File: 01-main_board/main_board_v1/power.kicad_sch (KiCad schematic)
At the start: 20 parts, among them IC1 MAX6105EUR+T, IC2 LP5907MFX-2.5_NOPB, IC3 L78M05ABDT-TR, IC4 SPX3819S-L_TR, U4 TPS2115APWR

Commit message: finished analog input traces
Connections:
- net GNDA is gone; now on net PGND: C38.2, C39.1, C41.1, C7.1, R45.2
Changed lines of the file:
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@@
 			)
 		)
-		(property "Value" "GNDA"
+		(property "Value" "PGND"
 			(at 127 121.92 0)
 			(effects
@@
 			)
 		)
-		(property "Value" "GNDA"
+		(property "Value" "PGND"
 			(at 78.74 63.5 0)
 			(effects
@@
 			)
 		)
-		(property "Value" "GNDA"
+		(property "Value" "PGND"
 			(at 124.46 93.98 0)
 			(effects
@@
 			)
 		)
-		(property "Value" "GNDA"
+		(property "Value" "PGND"
 			(at 76.2 95.25 0)
 			(effects
@@
 			)
 		)
-		(property "Value" "GNDA"
+		(property "Value" "PGND"
 			(at 76.2 118.11 0)
 			(effects

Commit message: resolved all non-GND related DRC issues in layout
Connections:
- net 3V3: no longer C1.1, IC2.1 (IN), IC2.3 (EN)
- new net 3V3_teensy: C1.1, IC2.1 (IN), IC2.3 (EN)
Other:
- moved on the sheet: D1
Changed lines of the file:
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@@
 	(text "ESP32 recommends 3.3V power supply with >= 500 mA supply current, \n\nESP32C6 or ESP32S3 specifically, dobule check datasheets\n"
 		(exclude_from_sim no)
-		(at 235.712 143.256 0)
+		(at 255.27 141.732 0)
 		(effects
 			(font
@@
 	(text "Vout = 1.235(1 + R1/R2), 22k < r2 < 47k, lower r1 to round\noutput capacitor is 2.2uF if alunimum and 1 uF if tantalum"
 		(exclude_from_sim no)
-		(at 237.49 107.95 0)
+		(at 251.46 133.096 0)
 		(effects
 			(font
@@
 	(text "Note: 2.5V Reference supplied by DAC"
 		(exclude_from_sim no)
-		(at 189.23 76.962 0)
+		(at 182.372 79.756 0)
 		(effects
 			(font
@@
 		)
 	)
-	(global_label "3V3"
+	(global_label "3V3_teensy"
 		(shape input)
 		(at 115.57 71.12 180)
@@
 		)
 		(property "Intersheetrefs" "${INTERSHEET_REFS}"
-			(at 109.0772 71.12 0)
-			(effects
-				(font
-					(size 1.27 1.27)
-				)
-				(justify right)
-				(hide yes)
-			)
-		)
-	)
-	(global_label "3V3"
+			(at 102.062 71.12 0)
+			(effects
+				(font
+					(size 1.27 1.27)
+				)
+				(justify right)
+				(hide yes)
+			)
+		)
+	)
+	(global_label "3V3_teensy"
 		(shape input)
-		(at 127 76.2 180)
-		(fields_autoplaced yes)
-		(effects
-			(font
-				(size 1.27 1.27)
-			)
-			(justify right)
-		)
-		(property "Intersheetrefs" "${INTERSHEET_REFS}"
-			(at 120.5072 76.2 0)
+		(at 127 76.2 270)
+		(fields_autoplaced yes)
+		(effects
+			(font
+				(size 1.27 1.27)
+			)
+			(justify right)
+		)
+		(property "Intersheetrefs" "${INTERSHEET_REFS}"
+			(at 127 89.708 90)
 			(effects
 				(font
@@
 	(global_label "11.1V"
 		(shape output)
-		(at 55.88 40.64 0)
+		(at 93.98 52.07 0)
 		(fields_autoplaced yes)
 		(effects
@@
 		)
 		(property "Intersheetrefs" "${INTERSHEET_REFS}"
-			(at 64.1871 40.64 0)
+			(at 102.2871 52.07 0)
 			(effects
 				(font
@@
 	(global_label "11.1V_battery"
 		(shape input)
-		(at 48.26 40.64 180)
-		(fields_autoplaced yes)
-		(effects
-			(font
-				(size 1.27 1.27)
-			)
-			(justify right)
-		)
-		(property "Intersheetrefs" "${INTERSHEET_REFS}"
-			(at 32.3935 40.64 0)
+		(at 86.36 52.07 180)
+		(fields_autoplaced yes)
+		(effects
+			(font
+				(size 1.27 1.27)
+			)
+			(justify right)
+		)
+		(property "Intersheetrefs" "${INTERSHEET_REFS}"
+			(at 70.4935 52.07 0)
 			(effects
 				(font
@@
 	(symbol
 		(lib_id "Device:D_Schottky")
-		(at 52.07 40.64 180)
+		(at 90.17 52.07 180)
 		(unit 1)
 		(exclude_from_sim no)
@@
 		(fields_autoplaced yes)
 		(property "Reference" "D1"
-			(at 52.3875 34.29 0)
+			(at 90.4875 45.72 0)
 			(effects
 				(font
@@
 		)
 		(property "Value" "D_Schottky"
-			(at 52.3875 36.83 0)
+			(at 90.4875 48.26 0)
 			(effects
 				(font
@@
 		)
 		(property "Footprint" "Diode_SMD:D_2114_3652Metric"
-			(at 52.07 40.64 0)
+			(at 90.17 52.07 0)
 			(effects
 				(font
@@
 		)
 		(property "Datasheet" "~"
-			(at 52.07 40.64 0)
+			(at 90.17 52.07 0)
 			(effects
 				(font
@@
 		)
 		(property "Description" "Schottky diode"
-			(at 52.07 40.64 0)
-			(effects
-				(font
+			(at 90.17 52.07 0)
+			(effects
+				(font

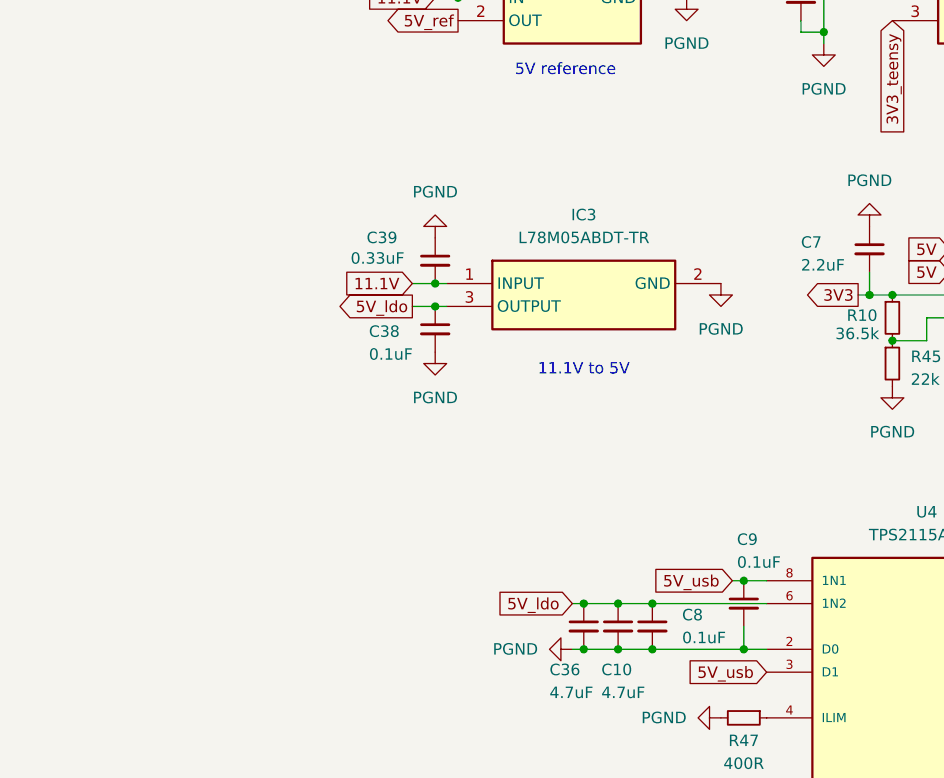
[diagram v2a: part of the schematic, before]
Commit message: changed 5V ldo to 5V buck
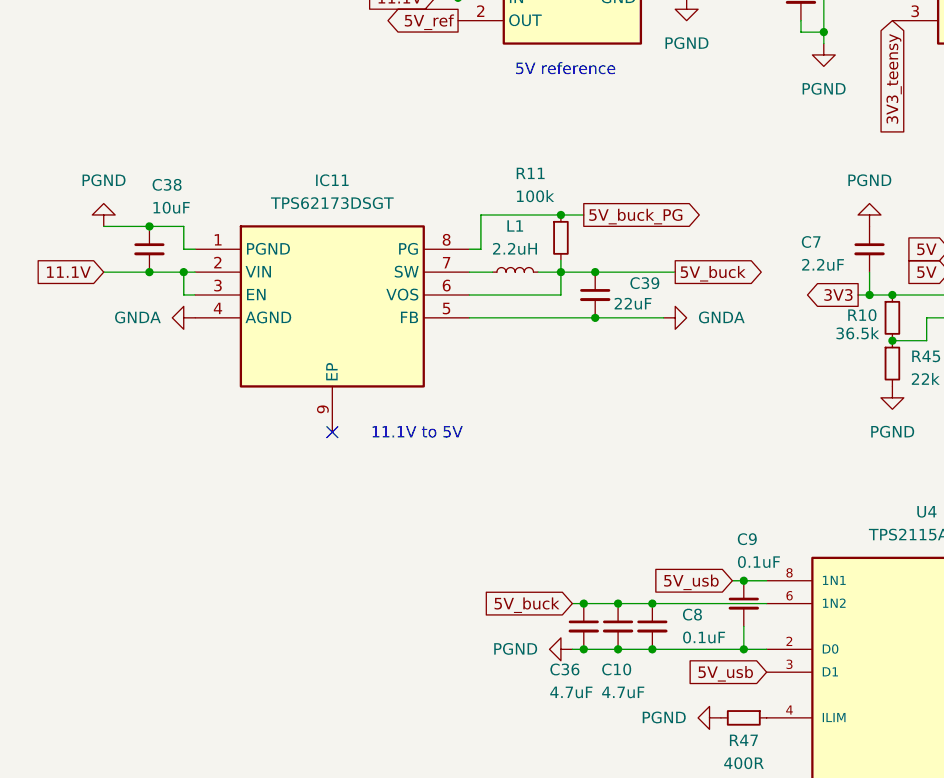
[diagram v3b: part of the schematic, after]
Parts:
- removed IC3: L78M05ABDT-TR, L78M05ABDTTR, symbol 22XT_Main:L78M05ABDT-TR
- added IC11: TPS62173DSGT, 22XT_Main:SON50P200X200X80-9N, symbol 22XT_Main:TPS62173DSGT
- added L1: 2.2uH, Inductor_SMD:L_0402_1005Metric, symbol Device:L_Small
- added R11: 100k, Resistor_SMD:R_0402_1005Metric, symbol Device:R_Small
- C38: value 0.1uF -> 10uF
- C39: value 0.33uF -> 22uF
- D1: footprint Diode_SMD:D_2114_3652Metric -> Diode_SMD:D_0402_1005Metric
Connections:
- net 11.1V: now also C38.2, IC11.2 (VIN), IC11.3 (EN); no longer C39.2
- net PGND: now also C38.1, IC11.1 (PGND); no longer C38.2, C39.1
- net 5V_ldo renamed 5V_buck
- net 5V_buck: now also C39.1, IC11.6 (VOS), L1.2, R11.2; no longer C38.1
- new net: IC11.7 (SW), L1.1
- new net 5V_buck_PG: IC11.8 (PG), R11.1
- new net GNDA: C39.2, IC11.4 (AGND), IC11.5 (FB)
- no-connect marks 0 -> 1
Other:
- moved on the sheet: C38, C39

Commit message: Emma revision
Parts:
- added NT1: NetTie_2, symbol Device:NetTie_2
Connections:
- net GNDA: now also NT1.1
- net PGND renamed B-
- net B-: now also NT1.2
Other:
- note added: "11.1V to 5V buck converter"
- note added: "3.3V to 2.5V LDO"
- note added: "5V to 3.3V LDO"
- note removed: "11.1V to 5V"
- note removed: "3.3V to 2.5V"
- note removed: "5V to 3.3V"

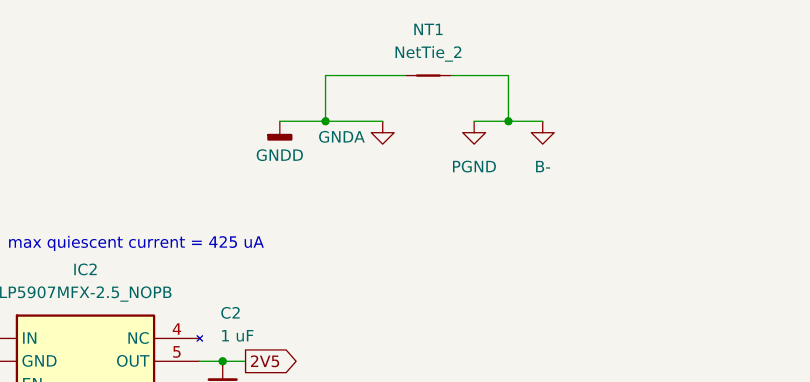
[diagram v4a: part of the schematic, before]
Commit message: Added main board footprint library
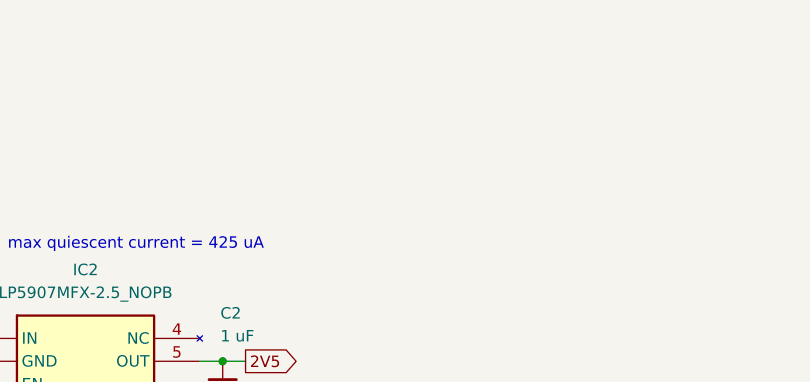
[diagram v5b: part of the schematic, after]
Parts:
- removed NT1: NetTie_2, symbol Device:NetTie_2
- IC1: footprint SOT95P229X119-3N -> (none)
- IC2: footprint SOT95P280X145-5N -> (none)
- IC4: footprint SOIC127P600X175-8N -> (none)
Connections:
- net B- renamed PGND

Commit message: Added new commit
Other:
- note added: "LSM115JE3/TR13:"
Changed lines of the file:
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@@
 	(generator_version "9.0")
 	(paper "A4")
+	(text "LSM115JE3/TR13:"
+		(exclude_from_sim no)
+		(at 91.186 42.926 0)
+		(effects
+			(font
+				(size 1.27 1.27)
+			)
+		)
+	)
 	(text "5V to 3.3V\nLDO"
 		(exclude_from_sim no)

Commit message: Re-assigned all footprints
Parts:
- D1: footprint Diode_SMD:D_0402_1005Metric -> 22XT_Main:DO-214BA_MCH
- IC1: footprint (none) -> Package_TO_SOT_SMD:SOT-23-3
- IC2: footprint (none) -> Package_TO_SOT_SMD:SOT-23-5
- IC4: footprint (none) -> 22XT_Main:SOIC127P600X175-8N
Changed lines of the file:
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@@
 			)
 		)
-		(property "Footprint" "Diode_SMD:D_0402_1005Metric"
+		(property "Footprint" "22XT_Main:DO-214BA_MCH"
 			(at 90.17 52.07 0)
 			(effects
@@
 			)
 		)
-		(property "Footprint" ""
+		(property "Footprint" "Package_TO_SOT_SMD:SOT-23-3"
 			(at 100.33 168.58 0)
 			(effects
@@
 			)
 		)
-		(property "Footprint" ""
+		(property "Footprint" "Package_TO_SOT_SMD:SOT-23-5"
 			(at 148.59 166.04 0)
 			(effects
@@
 			)
 		)
-		(property "Footprint" ""
+		(property "Footprint" "22XT_Main:SOIC127P600X175-8N"
 			(at 160.02 196.52 0)
 			(effects

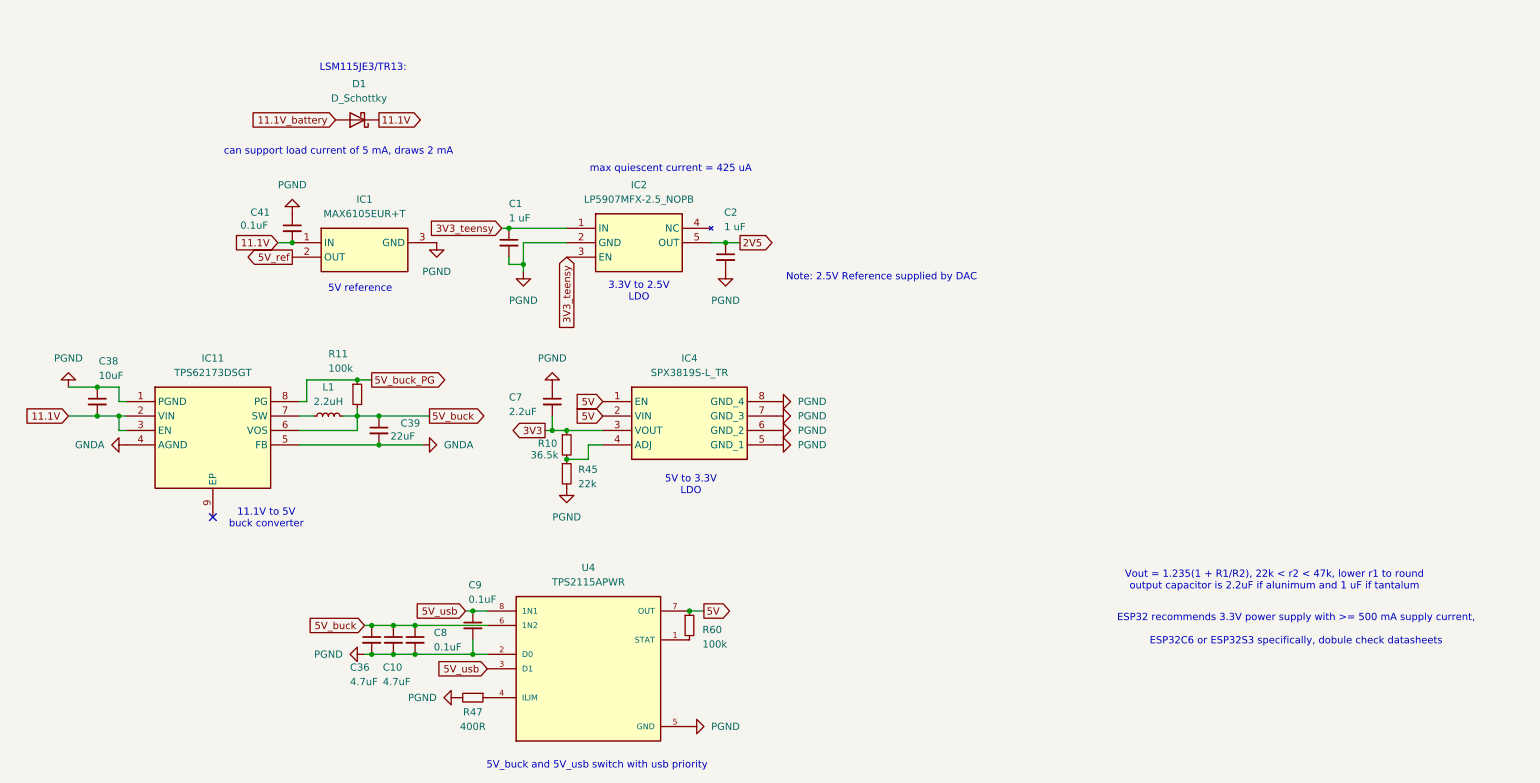
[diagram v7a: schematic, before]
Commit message: added supply test flags, gnd planes, fixed silkscreen overlaps
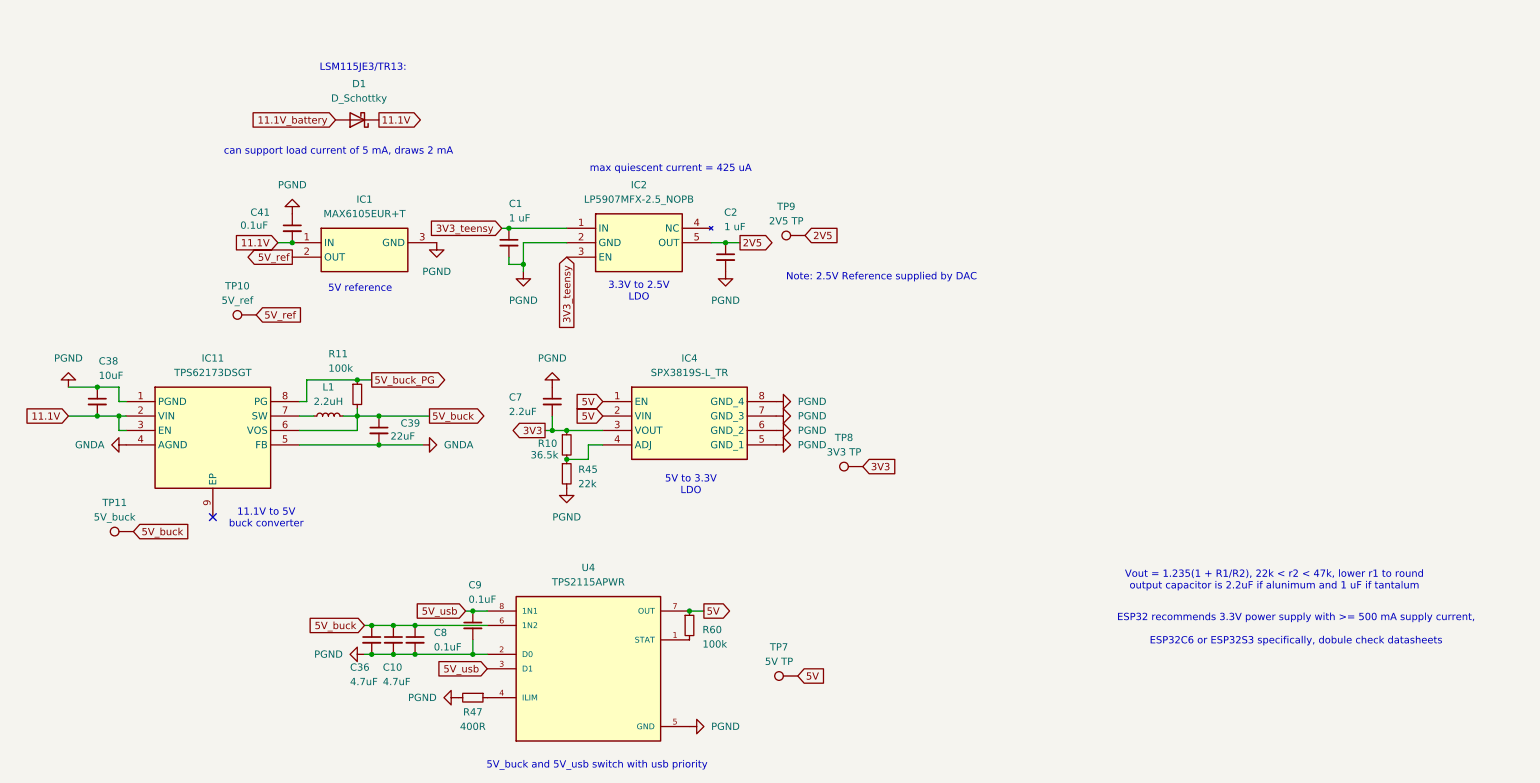
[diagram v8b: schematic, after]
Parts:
- added TP10: 5V_ref, TestPoint:TestPoint_Pad_1.0x1.0mm, symbol Connector:TestPoint
- added TP11: 5V_buck, TestPoint:TestPoint_Pad_1.0x1.0mm, symbol Connector:TestPoint
- added TP7: 5V TP, TestPoint:TestPoint_Pad_1.0x1.0mm, symbol Connector:TestPoint
- added TP8: 3V3 TP, TestPoint:TestPoint_Pad_1.0x1.0mm, symbol Connector:TestPoint
- added TP9: 2V5 TP, TestPoint:TestPoint_Pad_1.0x1.0mm, symbol Connector:TestPoint
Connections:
- net 2V5: now also TP9.1
- net 3V3: now also TP8.1
- net 5V: now also TP7.1
- net 5V_buck: now also TP11.1
- net 5V_ref: now also TP10.1
